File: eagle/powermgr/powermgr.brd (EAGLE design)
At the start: 100 x 80 mm, 18 parts, among them IC1 PIC16F1455, IC2 4027D, IC3 MCP1703DB, Q1 BSS123, Q2 BSS123, X1 MINI-USB-32005-201

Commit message: First pass of power management board completed
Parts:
- added C10, C9: .1u, resistor:C0603K
- added C11, C8: 10n, resistor:C0603K
- added C7: 0.1u, resistor:C1206K
- added IC4: ACS756, custom:5PFF
- added JP5: (no value), pinhead:1X02
- added JP6: (no value), pinhead:1X06
- added R3: 1k, resistor:R0603
- added R4: 50k, resistor:R0603
- added R5, R6: 10k, resistor:R0603
- added R7: 220, resistor:R0603
- added X2: (no value), con-wago-500:W237-4
- C3: value (none) -> 47u; device resistor:C0805 -> resistor:E2,5-6
- C4, C5: value (none) -> .1u
- C6: value (none) -> 1u
- IC1: value PIC16F1455 -> PIC16F1455TSSOP-14; device custom:SOIC-14 -> custom:TSSOP-14
- IC3: value MCP1703DB -> MCP1804
- X1: value MINI-USB-32005-201 -> 10104111-0001LF; device con-cypressindustries:32005-201 -> custom:USBAB
- moved JP2 58.4 mm to (76.2, 31.8)
- moved R2 57.1 mm to (69.1, 31.8), turned to 90 degrees
- moved IC1 56.3 mm to (67.6, 12.7), turned to 270 degrees
- moved C6 55.3 mm to (61.5, 4.83), turned to 180 degrees
- moved C5 53.5 mm to (61.5, 2.79), turned to 180 degrees
- moved X1 51.4 mm to (72.1, 2.29)
- moved IC2 50.0 mm to (66.5, 23.1)
- moved C3 49.6 mm to (45.5, 6.10), turned to 90 degrees
- moved C2 46.6 mm to (71.1, 31.8), turned to 90 degrees
- moved JP4 45.7 mm to (50.8, 31.8)
- moved Q1 44.3 mm to (48.0, 25.4)
- moved C4 42.2 mm to (50.0, 5.84), turned to 270 degrees
- moved JP1 39.4 mm to (63.5, 31.8)
- moved R1 38.4 mm to (56.4, 31.8), turned to 90 degrees
- moved IC3 33.8 mm to (55.1, 5.84)
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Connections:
- new net CURRENT: C8.1, IC1.7, R3.2
- new net N$10: C11.1, IC1.8, R4.1, R5.2
- new net N$11: JP6.1, R6.2, R7.2
- new net N$5: IC4.4, X2.1, X2.2
- new net N$6: IC4.5, X2.3, X2.4
- new net N$9: IC4.3, R3.1
- net !MCLR: now also R7.1
- net +24V: now also C3.+, JP5.1, R4.2; no longer C3.2
- net +5V: now also C10.2, C7.1, C9.1, IC4.1, JP6.2, R6.1; no longer X1.1
- net GND: now also C10.1, C11.2, C3.-, C7.2, C8.2, C9.2, IC4.2, JP5.2, JP6.3, R5.1; no longer C3.1
- net ICSPCLK: now also JP6.5
- net ICSPDAT: now also JP6.4
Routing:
- net +5V: track 0.00 -> 134.3 mm, vias 0 -> 3
- net +24V: track 0.00 -> 66.3 mm
- net GND: track 0.00 -> 41.4 mm, vias 0 -> 15
- net PWR: track 0.00 -> 30.2 mm, vias 0 -> 3
- net CURRENT: track 0.00 -> 29.9 mm
- net ICSPCLK: track 0.00 -> 25.2 mm, vias 0 -> 2
- net KILL: track 0.00 -> 25.2 mm
- net N$10: track 0.00 -> 22.8 mm
- net ICSPDAT: track 0.00 -> 20.5 mm, vias 0 -> 2
- net N$1: track 0.00 -> 19.4 mm, vias 0 -> 1
- net !MCLR: track 0.00 -> 13.0 mm, vias 0 -> 2
- net N$2: track 0.00 -> 12.3 mm
- net N$3: track 0.00 -> 10.8 mm
- net USBD-: track 0.00 -> 6.56 mm
- net USBD+: track 0.00 -> 6.56 mm
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- added copper zone on layer 16, net GND
- added copper zone on layer 1, net N$5
- added copper zone on layer 16, net N$5
- added copper zone on layer 1, net N$6
- added copper zone on layer 16, net N$6
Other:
- board size 100 x 80 mm -> 88.9 x 38.1 mm

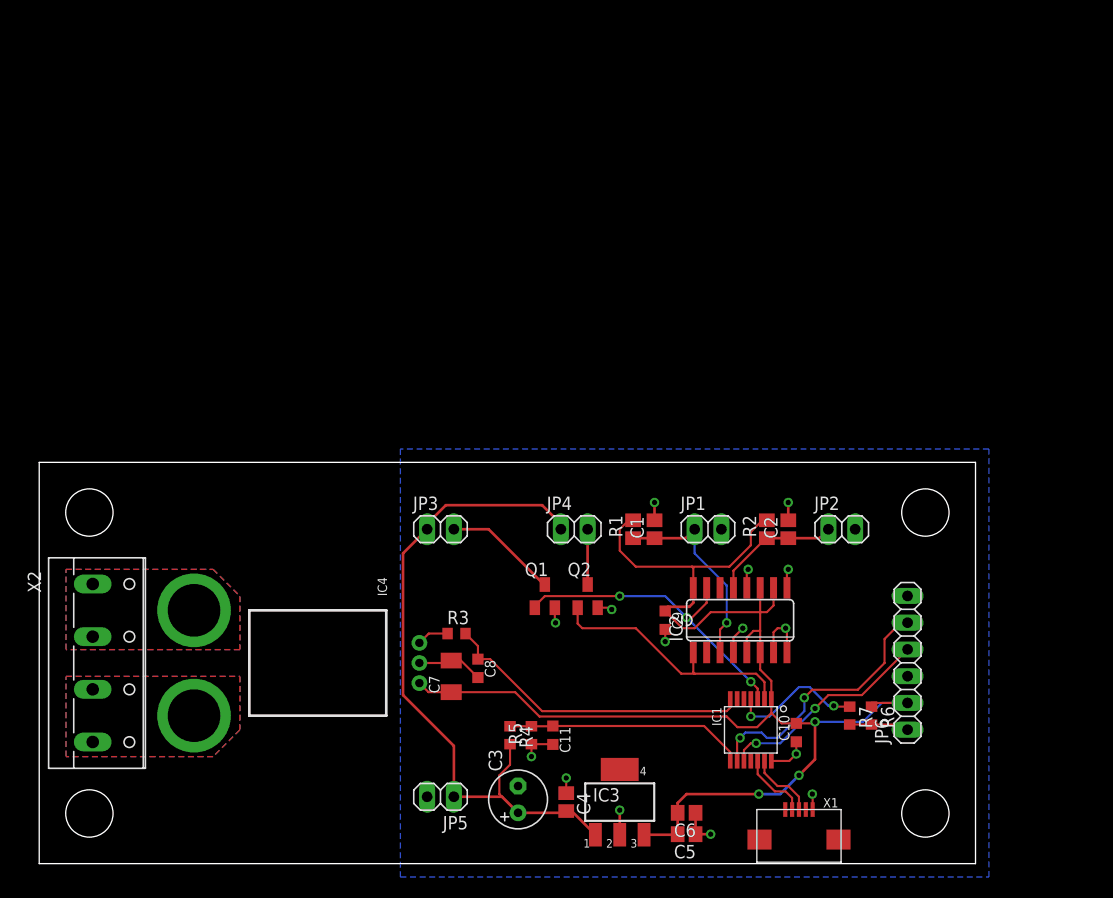
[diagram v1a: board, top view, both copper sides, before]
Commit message: Added LEDs, finalized silkscreen
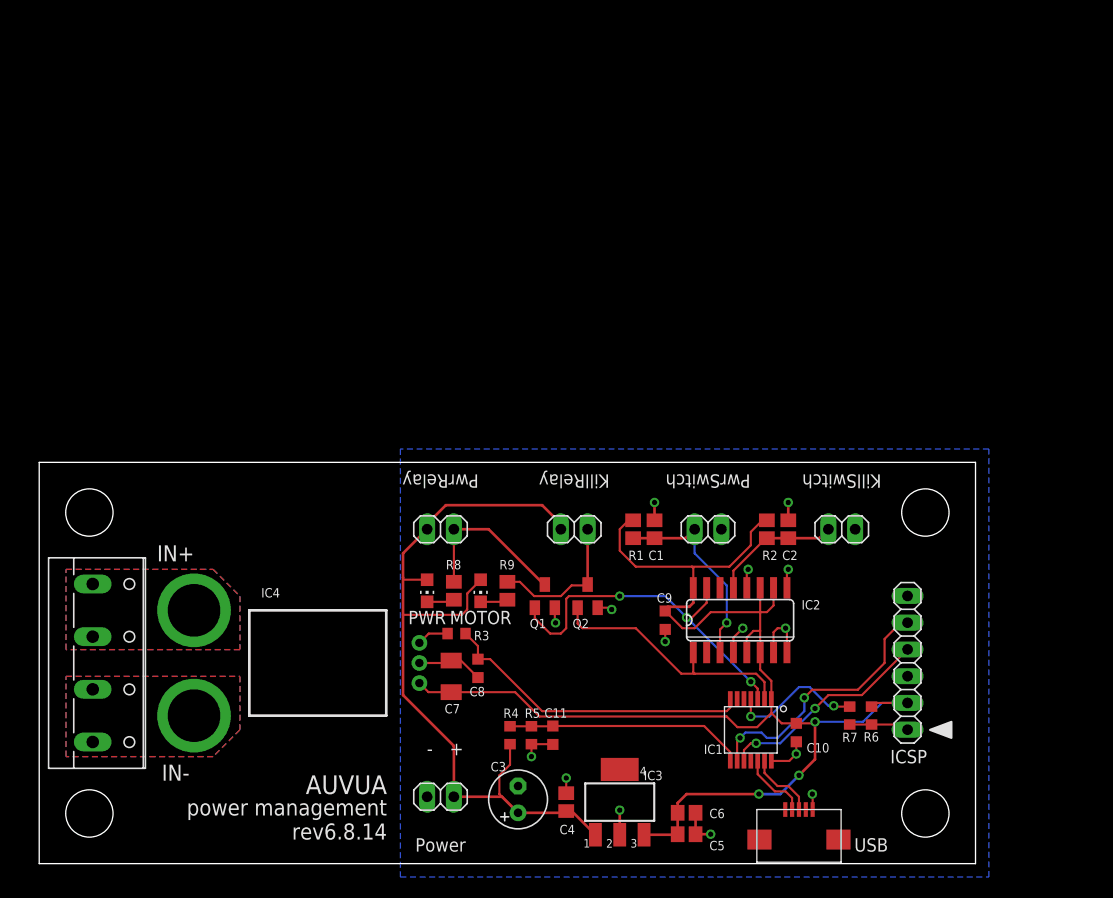
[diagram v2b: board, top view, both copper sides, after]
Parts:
- added MOTOR, PWR: (no value), led:CHIP-LED0805
- added R8, R9: 2.1k, resistor:R0805
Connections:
- new net N$12: MOTOR.C, R9.2
- new net N$7: PWR.C, R8.2
- net +24V: now also MOTOR.A, PWR.A
- net N$3: now also R8.1
- net N$4: now also R9.1
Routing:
- net +24V: track 66.3 -> 78.4 mm
- net N$4: track 5.25 -> 13.9 mm
- net N$3: track 10.8 -> 15.8 mm
- net PWR: track 30.2 -> 34.5 mm
- net N$7: track 0.00 -> 2.74 mm
- net N$12: track 0.00 -> 2.62 mm
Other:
- board text added: "+"
- board text added: "-"
- board text added: "AUVUA"
- board text added: "ICSP"
- board text added: "IN+"
- board text added: "IN-"
- board text added: "KillRelay"
- board text added: "KillSwitch"
- board text added: "Power"
- board text added: "PwrRelay"
- board text added: "PwrSwitch"
- board text added: "USB"
- board text added: "power management"
- board text added: "rev6.8.14"
